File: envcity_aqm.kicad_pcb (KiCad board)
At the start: 2 copper layers, 195.2 x 56 mm, 50 parts, among them J1 Conn_01x02_Male, J11 Conn_01x03_Female, J12 Conn_02x20_Odd_Even, J2 Conn_01x02_Male, J3 Conn_01x02_Female, J4 Conn_01x06_Male, J5 Conn_01x06_Male, J6 Conn_01x06_Male, J7 Conn_01x06_Male, J8 Conn_01x06_Male, J9 Conn_01x06_Male, Q1 BSS138, Q2 BSS138, Q3 BSS138, U1 BQ24160RGET, U2 ADS1115IDGST, U3 CD74HC4067M, U4 DHT11, U5 BUCK_BOOST_BOARD, U6 LM7805_TO220, U8 LM1117-3.3

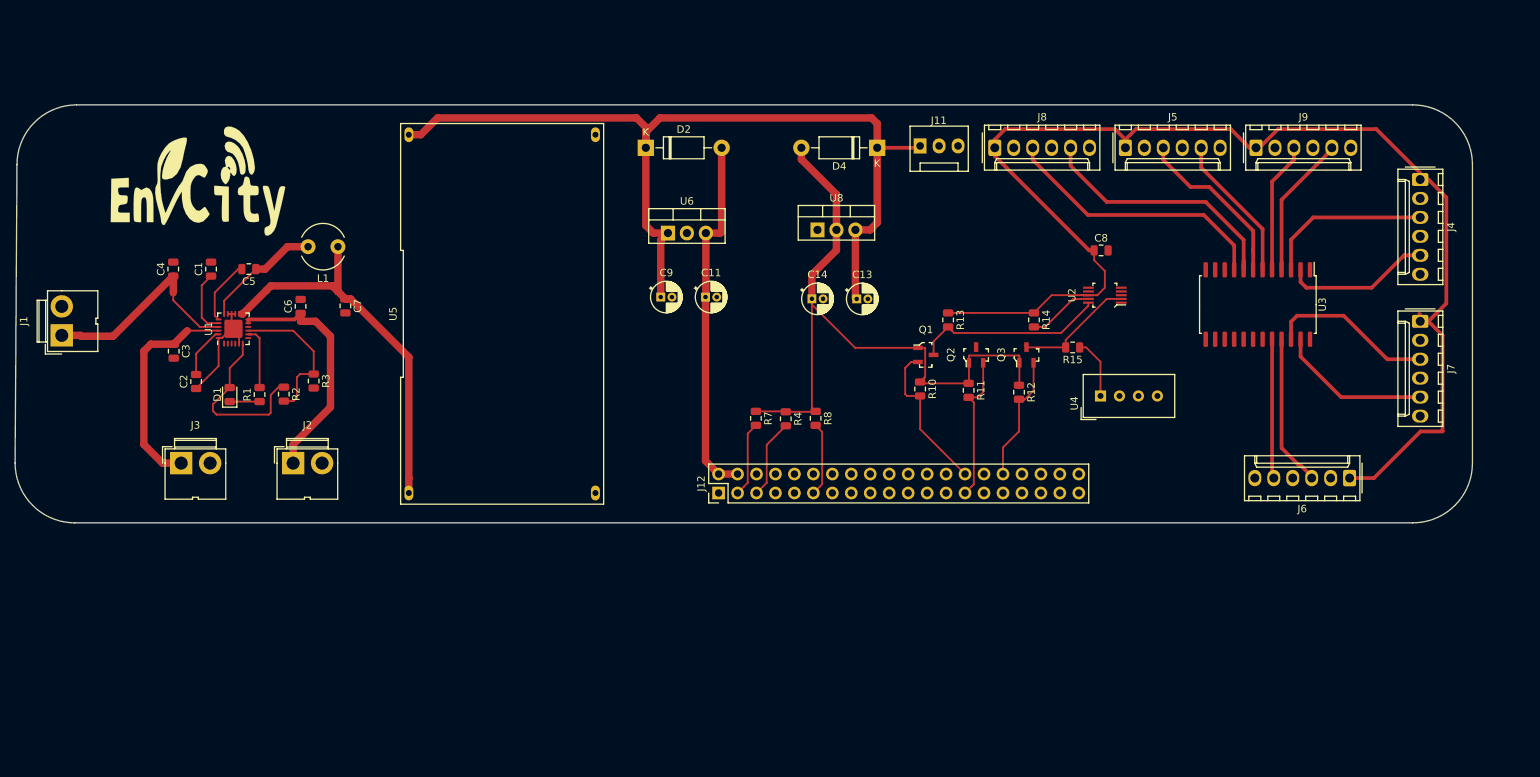
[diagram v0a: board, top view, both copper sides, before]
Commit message: Adicionando radio LoRa. Criando um .sch para a Raspberry e para o radio
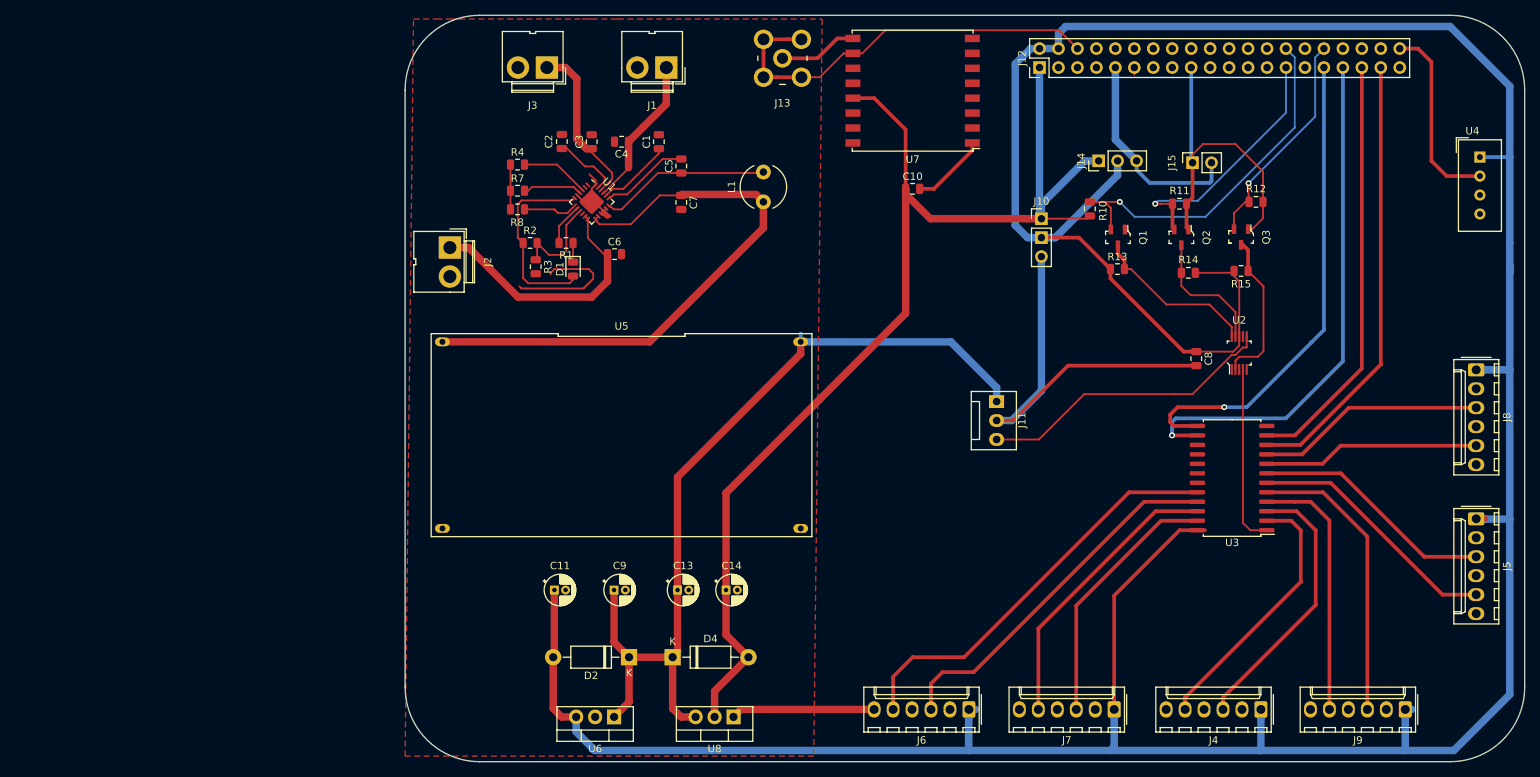
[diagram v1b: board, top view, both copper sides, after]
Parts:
- removed G***: LOGO, lib_logos:logo_big_neg
- added C10: 100nF, Capacitor_SMD:C_0805_2012Metric, F.Cu at (139.0, 68.2)
- added J10: Conn_01x03_Male, Connector_PinHeader_2.54mm:PinHeader_1x03_P2.54mm_Vertical, F.Cu at (156.2, 72.2)
- added J13: 5-1814400-1, digikey-footprints:RF_SMA_RightAngle_5-1814400-1, F.Cu at (121.6, 50.8)
- added J14: Conn_01x03_Male, Connector_PinHeader_2.54mm:PinHeader_1x03_P2.54mm_Vertical, F.Cu at (163.9, 64.5)
- added J15: Conn_01x02_Male, Connector_PinSocket_2.54mm:PinSocket_1x02_P2.54mm_Vertical, F.Cu at (176.5, 64.8)
- added U7: RFM95W-915S2, RF_Module:HOPERF_RFM9XW_SMD, F.Cu at (139.0, 55.1)
- moved J1 88.6 mm to (106.0, 52.0), turned to 180 degrees
- moved J9 77.9 mm to (205.0, 138.0), turned to 180 degrees
- moved J4 74.1 mm to (185.7, 138.0), turned to 180 degrees
- moved D4 73.5 mm to (106.8, 131.0), turned to 0 degrees
- moved J3 72.2 mm to (90.0, 52.0), turned to 180 degrees
- moved J12 71.4 mm to (156.0, 52.0)
- moved J8 71.0 mm to (214.5, 92.5), turned to 270 degrees
- moved J5 68.4 mm to (214.5, 112.5), turned to 270 degrees
- moved D2 68.3 mm to (101.0, 131.0), turned to 180 degrees
- moved J7 66.2 mm to (166.0, 138.0), turned to 180 degrees
- moved U8 66.2 mm to (115.0, 139.0), turned to 180 degrees
- moved U6 65.2 mm to (99.0, 139.0), turned to 180 degrees
- moved C3 62.6 mm to (96.0, 61.9), turned to 90 degrees
- moved C4 62.4 mm to (100.0, 61.9), turned to 180 degrees
- moved C1 62.4 mm to (105.0, 61.9)
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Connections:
- net Net-(C2-Pad2) renamed /Gerenciamento de Bateria/PMIDU
- J11 pad 3: AIN1 -> AIN2
- J12 pad 1: (no net) -> +3V3
- J12 pad 11: /Gerenciamento de Bateria/BQ_INT -> /BQ_INT
- J12 pad 12: (no net) -> /DIO4
- J12 pad 13: /Sensores/DHT_OUT -> /RESET
- J12 pad 14: (no net) -> GND
- J12 pad 15: (no net) -> /DIO0
- J12 pad 16: /S0 -> /DIO1
- J12 pad 17: (no net) -> +3V3
- J12 pad 18: /S1 -> /DIO3
- J12 pad 19: (no net) -> /SPI0_0
- J12 pad 20: (no net) -> GND
- J12 pad 21: (no net) -> /SPI0_1
- J12 pad 22: /S2 -> /DIO2
- J12 pad 23: (no net) -> /SPI0_2
- J12 pad 25: (no net) -> GND
- J12 pad 3: /Gerenciamento de Bateria/BQ_SDA -> /BQ_SDA
- J12 pad 30: (no net) -> GND
- J12 pad 31: (no net) -> /S3
- J12 pad 33: (no net) -> /S2
- J12 pad 34: (no net) -> GND
- J12 pad 35: (no net) -> /S1
- J12 pad 37: /S3 -> /S0
- J12 pad 38: (no net) -> /NSS
- J12 pad 39: (no net) -> GND
- J12 pad 40: (no net) -> /DHT22
- J12 pad 5: /Gerenciamento de Bateria/BQ_SCL -> /BQ_SCL
- J12 pad 6: (no net) -> GND
- J12 pad 9: (no net) -> GND
- J7 pad 3: /I9 -> /I8
- J7 pad 5: /I8 -> /I9
- R4 pad 2: /Gerenciamento de Bateria/BQ_SCL -> /BQ_SCL
- R7 pad 2: /Gerenciamento de Bateria/BQ_SDA -> /BQ_SDA
- R8 pad 2: /Gerenciamento de Bateria/BQ_INT -> /BQ_INT
- U1 pad 25: GND -> (no net)
- U1 pad 3: (no net) -> /BQ_SCL
- U1 pad 4: (no net) -> /BQ_SDA
- U1 pad 7: (no net) -> /BQ_INT
- U2 pad 5: AIN1 -> (no net)
- U2 pad 6: (no net) -> AIN2
- U4 pad 2: /Sensores/DHT_OUT -> /DHT22
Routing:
- net +5V: track 227.0 -> 470.5 mm
- net GND: track 15.9 -> 197.4 mm
- net +3V3: track 91.3 -> 213.6 mm
- net /S2: track 0.00 -> 70.8 mm, vias 0 -> 1
- net /S3: track 0.00 -> 65.5 mm, vias 0 -> 1
- net /S0: track 0.00 -> 59.5 mm
- net /S1: track 0.00 -> 56.8 mm
- net AIN2: track 0.00 -> 40.1 mm
- net /I11: track 18.7 -> 55.6 mm
- net /RASP_SCL0: track 20.6 -> 50.7 mm, vias 0 -> 1
- net /I10: track 20.4 -> 49.2 mm
- net /Reguladores/Vin: track 52.1 -> 78.3 mm
- net /DHT22: track 0.00 -> 25.6 mm
- net /ADS1115+MUX/AIN0: track 0.00 -> 24.2 mm
- net /I4: track 17.6 -> 39.1 mm
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- added copper zone on F.Cu, net GND
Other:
- board size 195.2 x 56 mm -> 150 x 100 mm

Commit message: Versão v0 finalizada. Adiciona pasta para os arquivos de saída e de fabricacao.
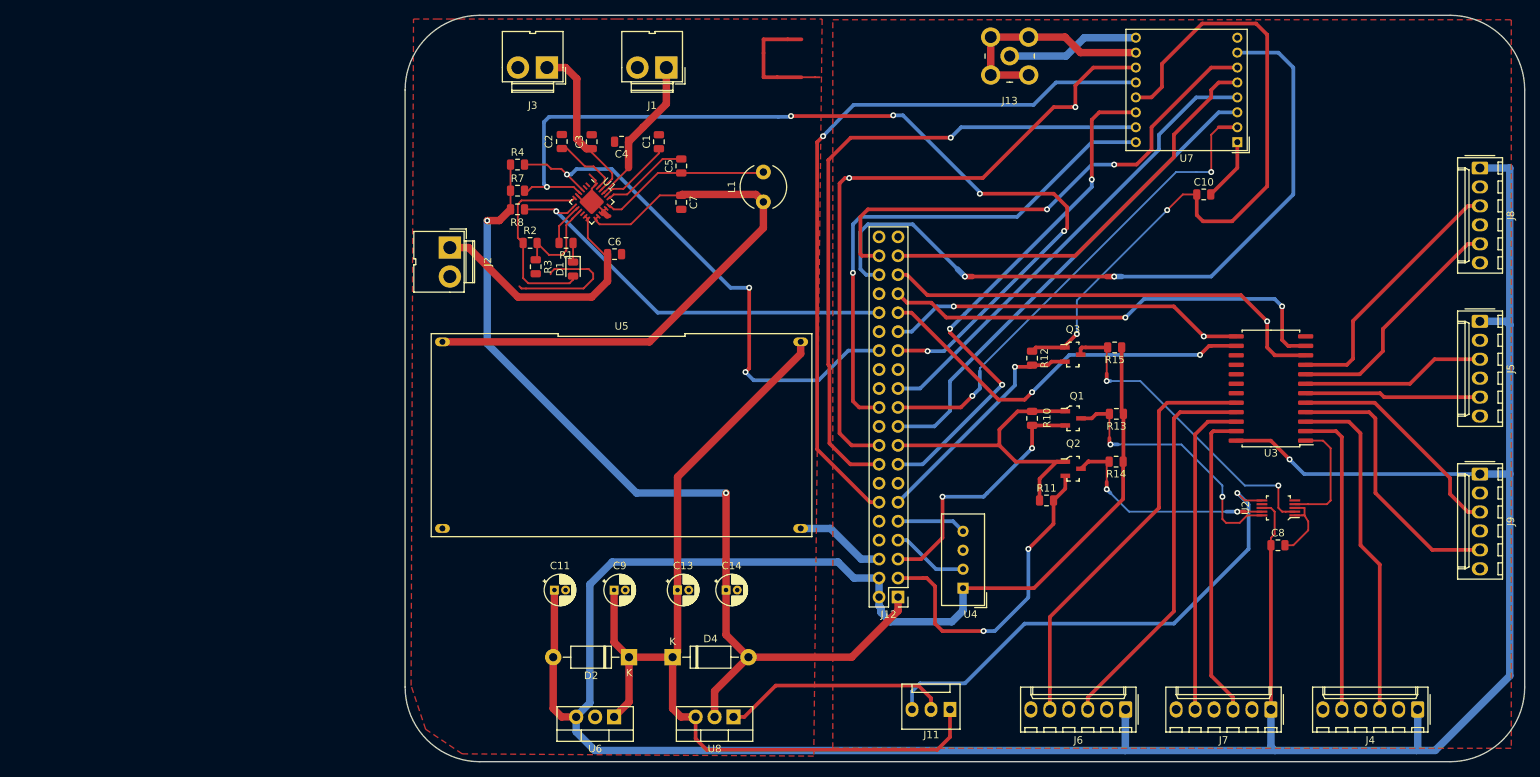
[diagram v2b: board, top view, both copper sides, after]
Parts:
- removed J10, J14: Conn_01x03_Male, Connector_PinHeader_2.54mm:PinHeader_1x03_P2.54mm_Vertical
- removed J15: Conn_01x02_Male, Connector_PinSocket_2.54mm:PinSocket_1x02_P2.54mm_Vertical
- U7: footprint RF_Module:HOPERF_RFM9XW_SMD -> RF_Module:HOPERF_RFM9XW_THT
- moved U4 90.2 mm to (145.8, 121.8), turned to 180 degrees
- moved J12 73.4 mm to (137.0, 122.9), turned to 180 degrees
- moved U7 44.0 mm to (182.5, 62.0)
- moved R11 43.6 mm to (156.9, 110.0), turned to 0 degrees
- moved J11 41.7 mm to (144.0, 138.0), turned to 180 degrees
- moved C10 39.0 mm to (178.0, 69.0)
- moved R12 36.6 mm to (155.0, 90.9), turned to 270 degrees
- moved Q2 34.2 mm to (160.5, 105.8), turned to 0 degrees
- moved J9 33.1 mm to (215.0, 106.5), turned to 270 degrees
- moved J13 30.4 mm to (152.0, 50.5)
- moved R10 29.1 mm to (155.0, 99.0), turned to 270 degrees
- moved Q3 27.5 mm to (160.4, 90.5), turned to 0 degrees
- moved C8 27.3 mm to (187.9, 116.0), turned to 0 degrees
- moved R14 27.1 mm to (166.3, 104.8)
- moved J8 27.0 mm to (215.0, 65.5)
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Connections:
- J12 pad 11: /BQ_INT -> /RASP_INT0
- J12 pad 13: /RESET -> (no net)
- J12 pad 27: /RASP_SDA0 -> /BQ_SDA
- J12 pad 28: /RASP_SCL0 -> /BQ_SCL
- J12 pad 29: (no net) -> /S3
- J12 pad 3: /BQ_SDA -> /RASP_SDA0
- J12 pad 31: /S3 -> /S2
- J12 pad 32: /RASP_INT0 -> /BQ_INT
- J12 pad 33: /S2 -> /S1
- J12 pad 35: /S1 -> /S0
- J12 pad 36: (no net) -> /DIO5
- J12 pad 37: /S0 -> /NSS
- J12 pad 38: /NSS -> /RESET
- J12 pad 40: /DHT22 -> (no net)
- J12 pad 5: /BQ_SCL -> /RASP_SCL0
- J12 pad 7: (no net) -> /DHT22
- U1 pad 25: (no net) -> GND
- U7 pad 7: (no net) -> /DIO5
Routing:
- net /BQ_SDA: track 8.15 -> 125.1 mm, vias 0 -> 6
- net /DIO5: track 0.00 -> 99.0 mm, vias 0 -> 2
- net /DIO4: track 0.00 -> 98.6 mm, vias 0 -> 1
- net /DIO1: track 0.00 -> 88.8 mm, vias 0 -> 1
- net /DIO3: track 0.00 -> 87.8 mm, vias 0 -> 2
- net /DIO0: track 0.00 -> 71.0 mm, vias 0 -> 3
- net /DIO2: track 0.00 -> 70.0 mm, vias 0 -> 1
- net /RESET: track 0.00 -> 68.1 mm, vias 0 -> 2
- net /SPI0_1: track 0.00 -> 65.5 mm, vias 0 -> 2
- net /SPI0_0: track 0.00 -> 65.2 mm
- net /BQ_SCL: track 9.19 -> 72.0 mm, vias 0 -> 3
- net /SPI0_2: track 0.00 -> 62.8 mm
- net /NSS: track 0.00 -> 57.4 mm
- net GND: track 197.4 -> 146.7 mm
- net /BQ_INT: track 7.96 -> 55.9 mm, vias 0 -> 1
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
